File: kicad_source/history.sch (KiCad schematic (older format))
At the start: 0 parts

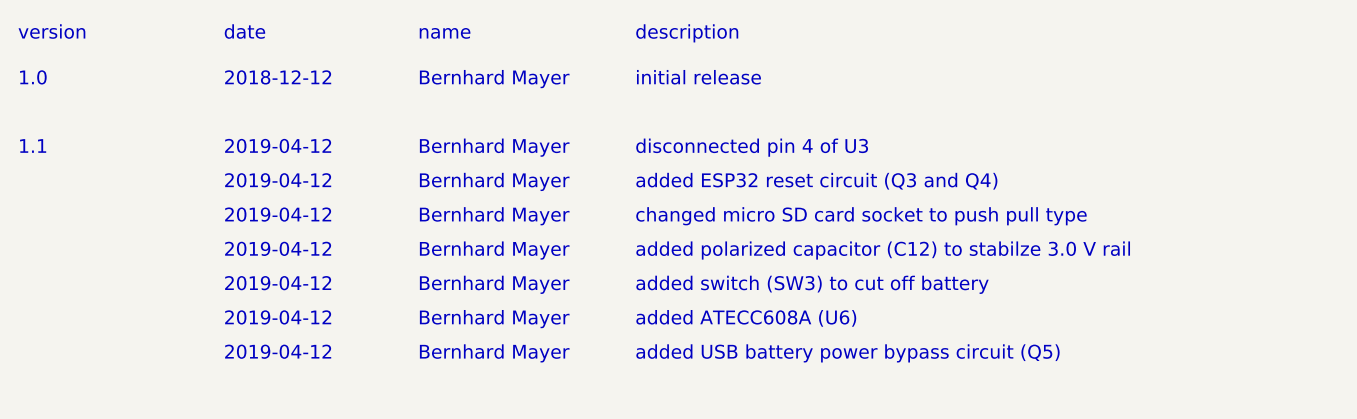
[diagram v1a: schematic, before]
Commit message: changed C9 to 10u (reset), updated schematic pdf
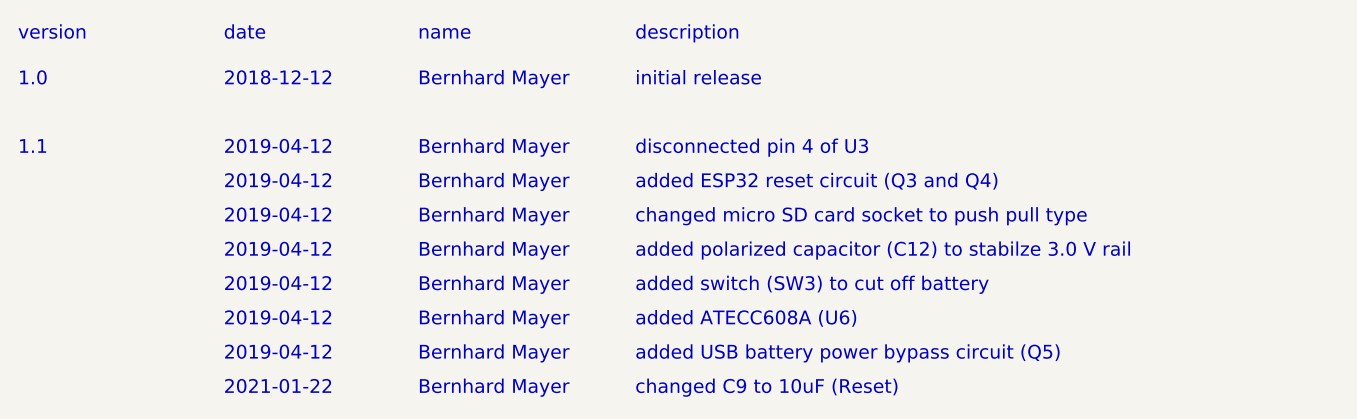
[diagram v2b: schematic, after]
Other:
- note added: "2021-01-22"
- note added: "changed C9 to 10uF (Reset)"
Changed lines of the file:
@@
 Sheet 2 3
 Title "Sensornator"
-Date "2019-04-12"
+Date "2021-01-22"
 Rev "1.1"
 Comp "generationmake"
@@
 Text Notes 1700 2200 0    60   ~ 0
 2019-04-12
+Text Notes 1700 2350 0    60   ~ 0
+2021-01-22
+Text Notes 2550 2350 0    60   ~ 0
+Bernhard Mayer
+Text Notes 3500 2350 0    60   ~ 0
+changed C9 to 10uF (Reset)
 $EndSCHEMATC
